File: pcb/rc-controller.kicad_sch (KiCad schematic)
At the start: 77 parts, among them J1 USB_C_Receptacle_USB2.0, M1 Motor_DC, Q1 AO3401A, Q2 AO3401A, Q3 AO3400A, Q4 AO3400A, SW1 SW_SPDT, SW2 SW_SPDT, SW3 SW_DPST, SW4 SW_DPST, SW5 SW_DPST, SW6 SW_DPST, U1 STM32F401RCTx, U2 LPS22HB, U3 SRV05-4, U4 TX4401, U5 ICM-42670-P, U6 TP4057-42, U7 nrf24L01P_PA_LNA, U8 SSD1306, Y1 16MHz

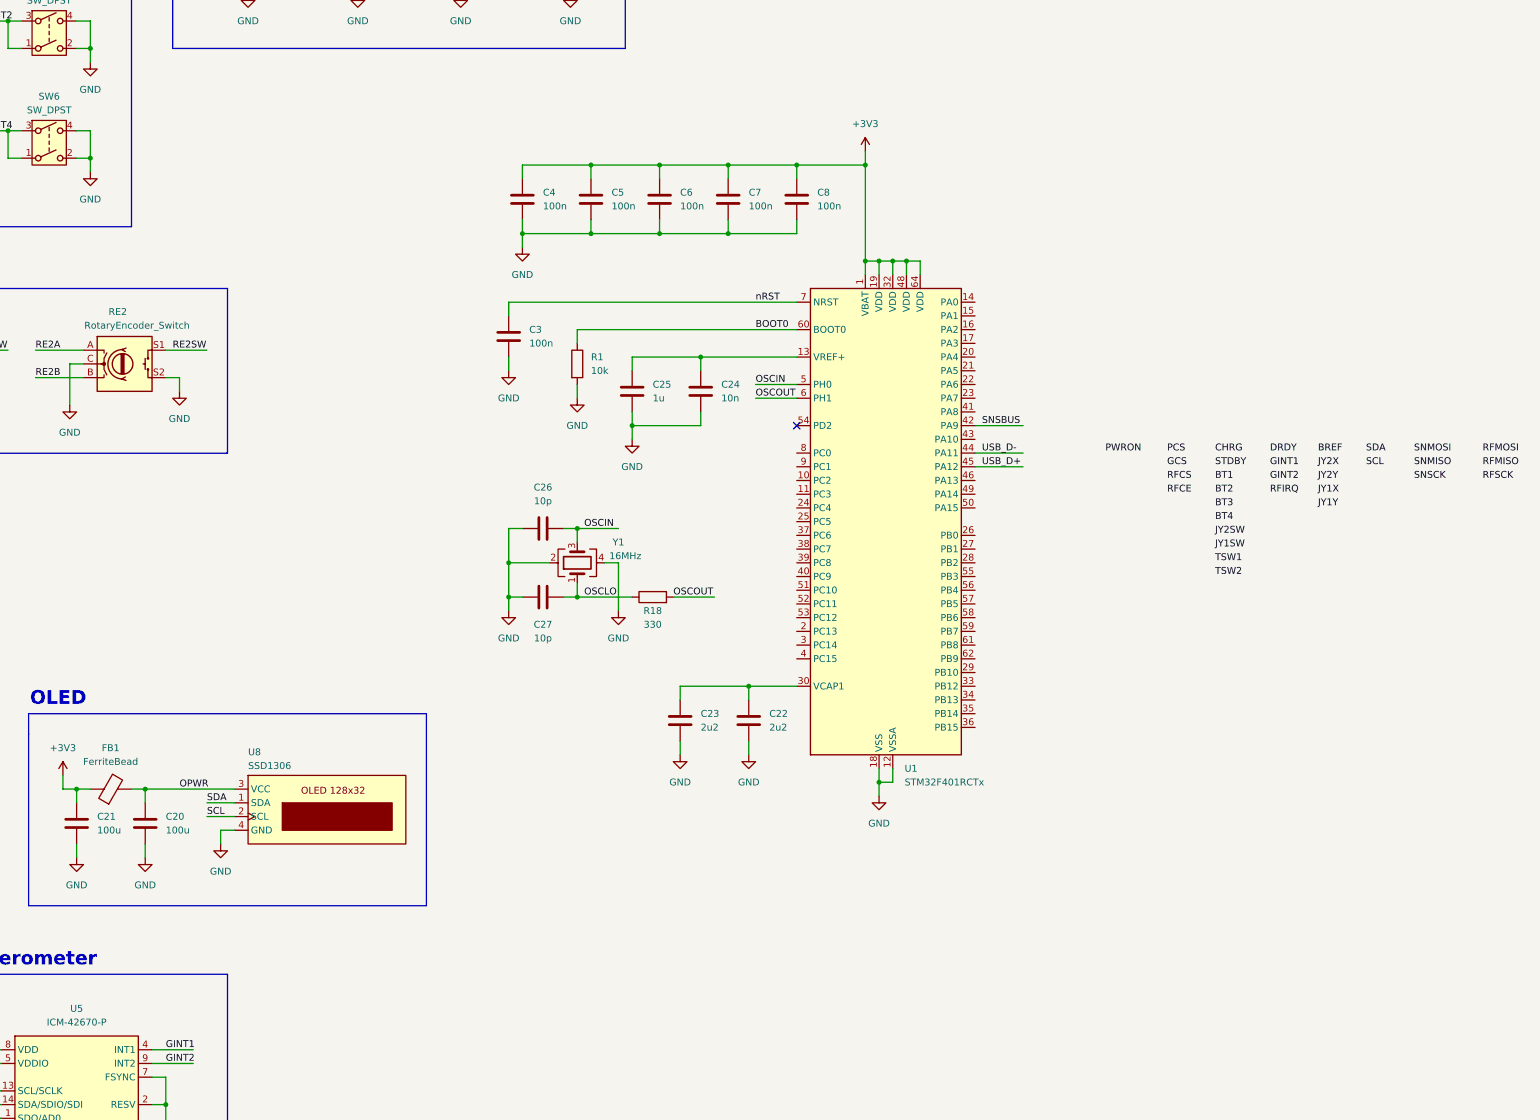
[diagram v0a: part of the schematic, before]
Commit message: Assign basic footprints
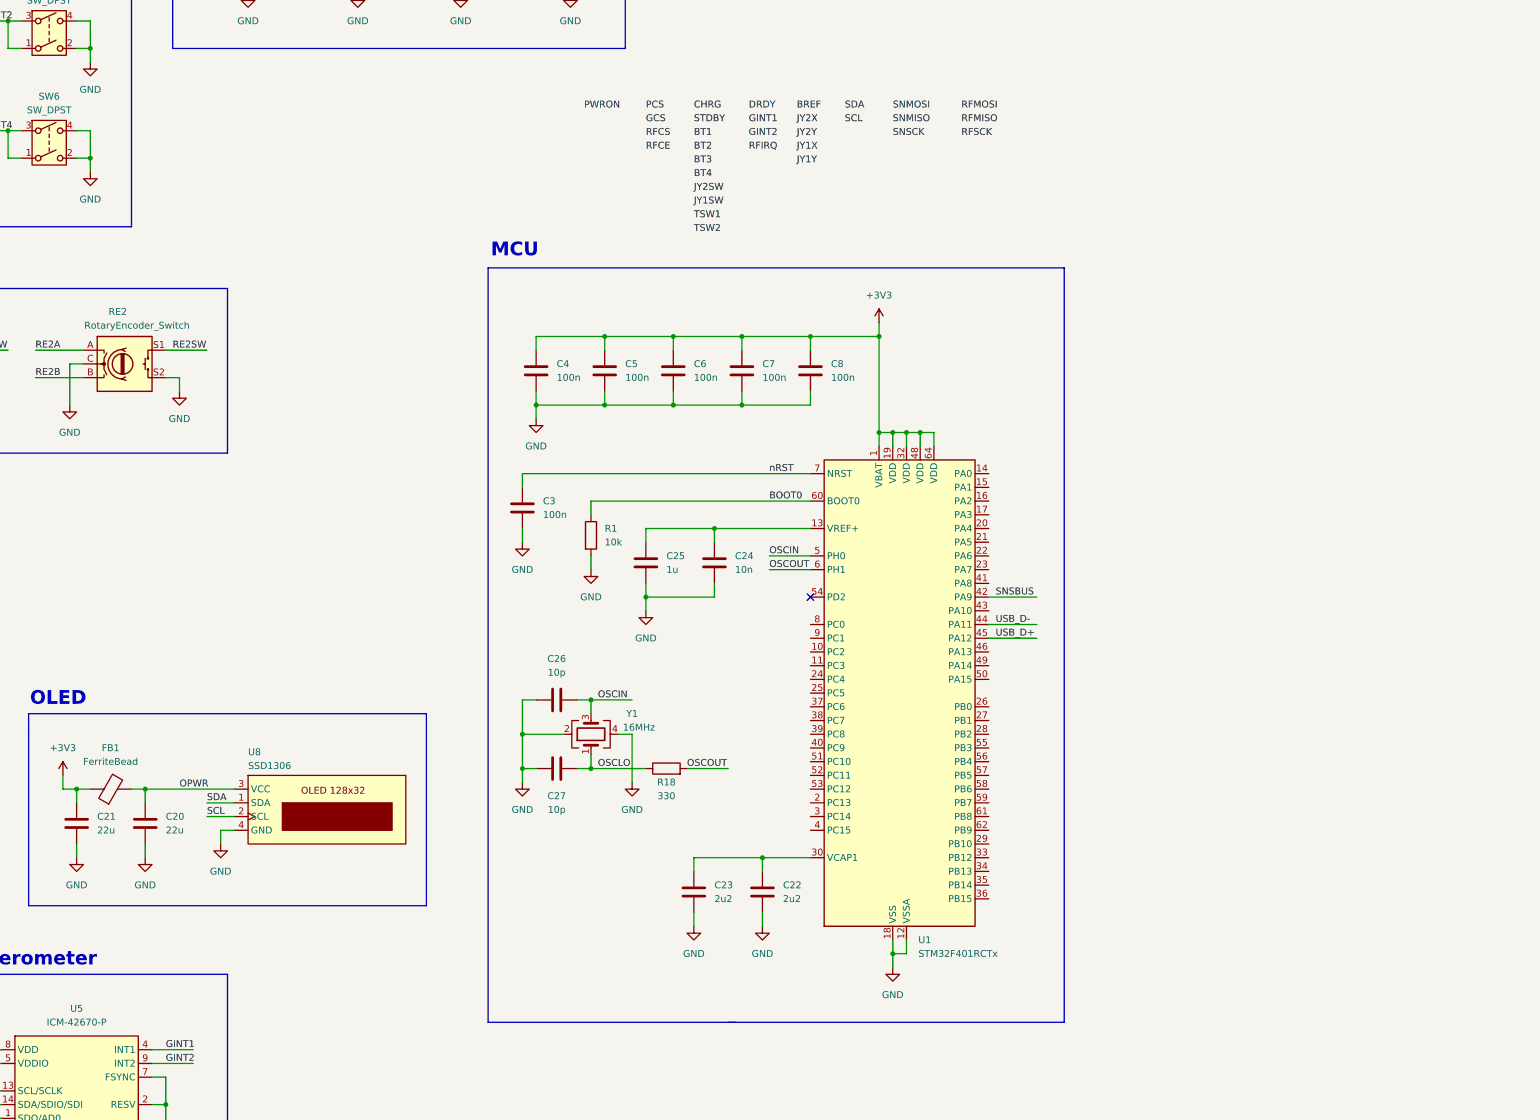
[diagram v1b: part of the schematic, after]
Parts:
- C1, C3, C4, C5, C6, C7, C8: footprint (none) -> Capacitor_SMD:C_0402_1005Metric
- C20, C21: value 100u -> 22u
- R11, R12, R13, R14, R16, R17, R9: footprint (none) -> Resistor_SMD:R_0402_1005Metric
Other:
- note added: "MCU"
- moved on the sheet: C22, C23, C24, C25, C26, C27, C3, C4, C5, C6, C7, C8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

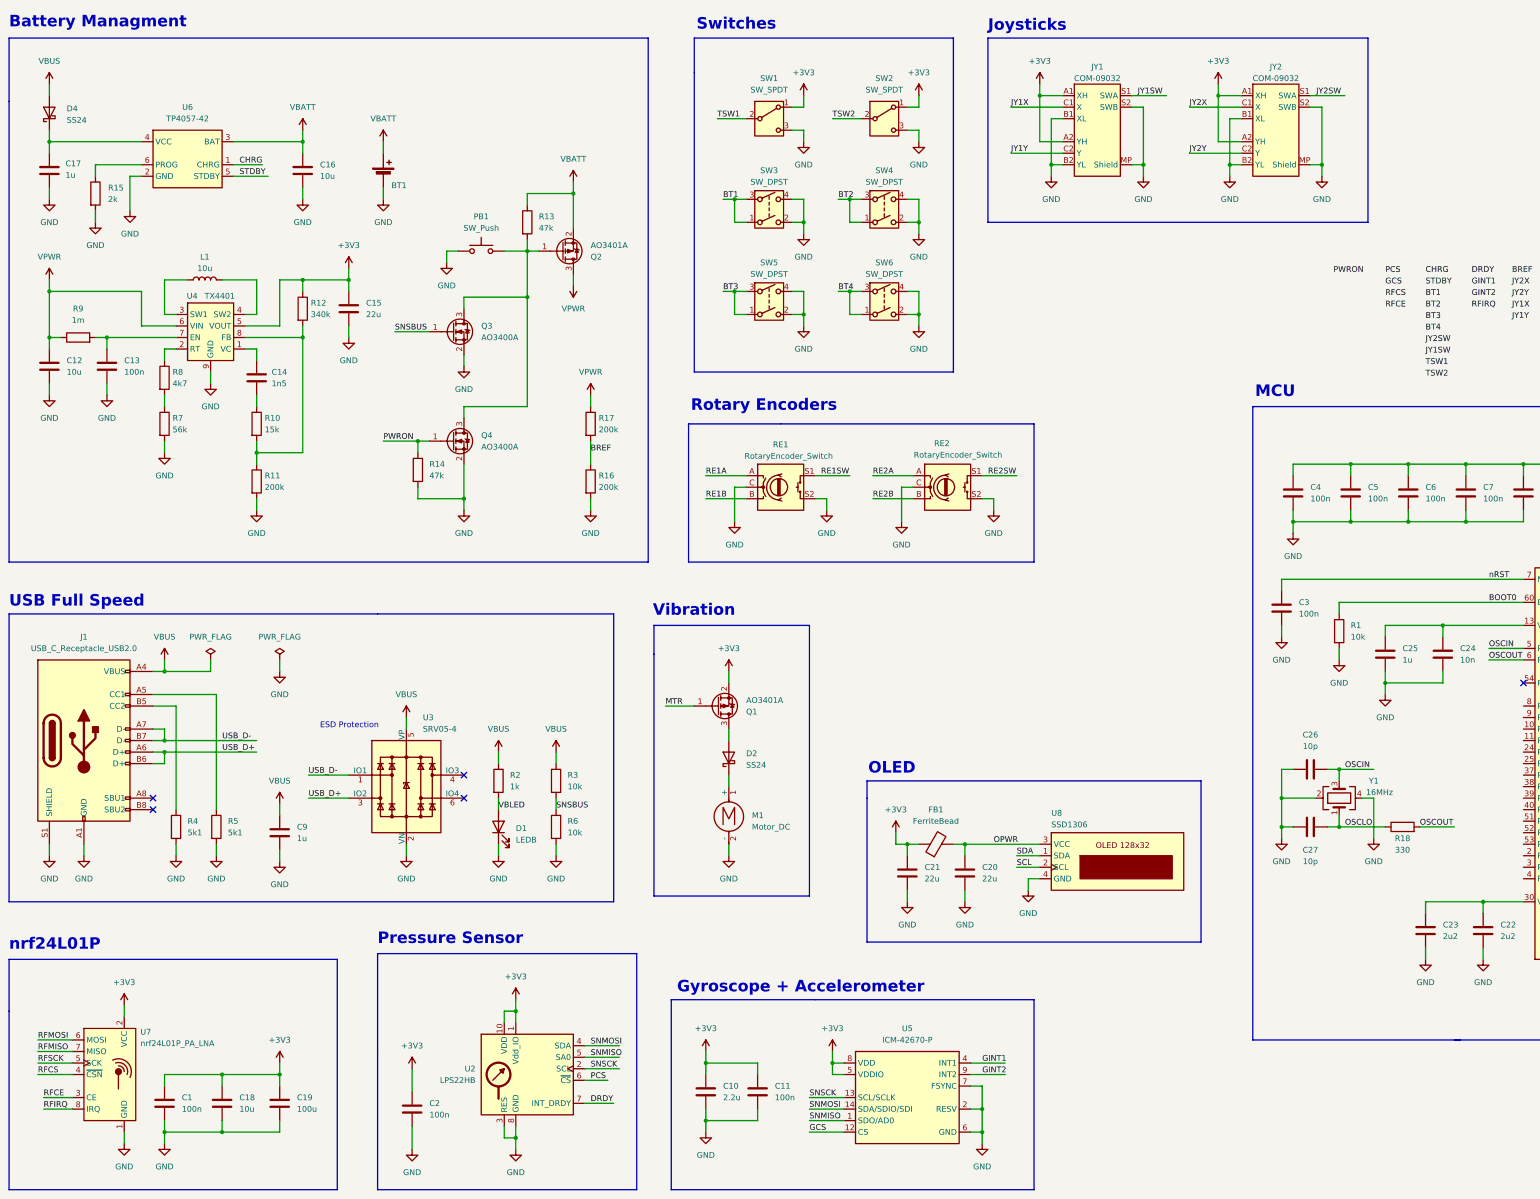
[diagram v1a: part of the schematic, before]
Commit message: Finish mapping footprints
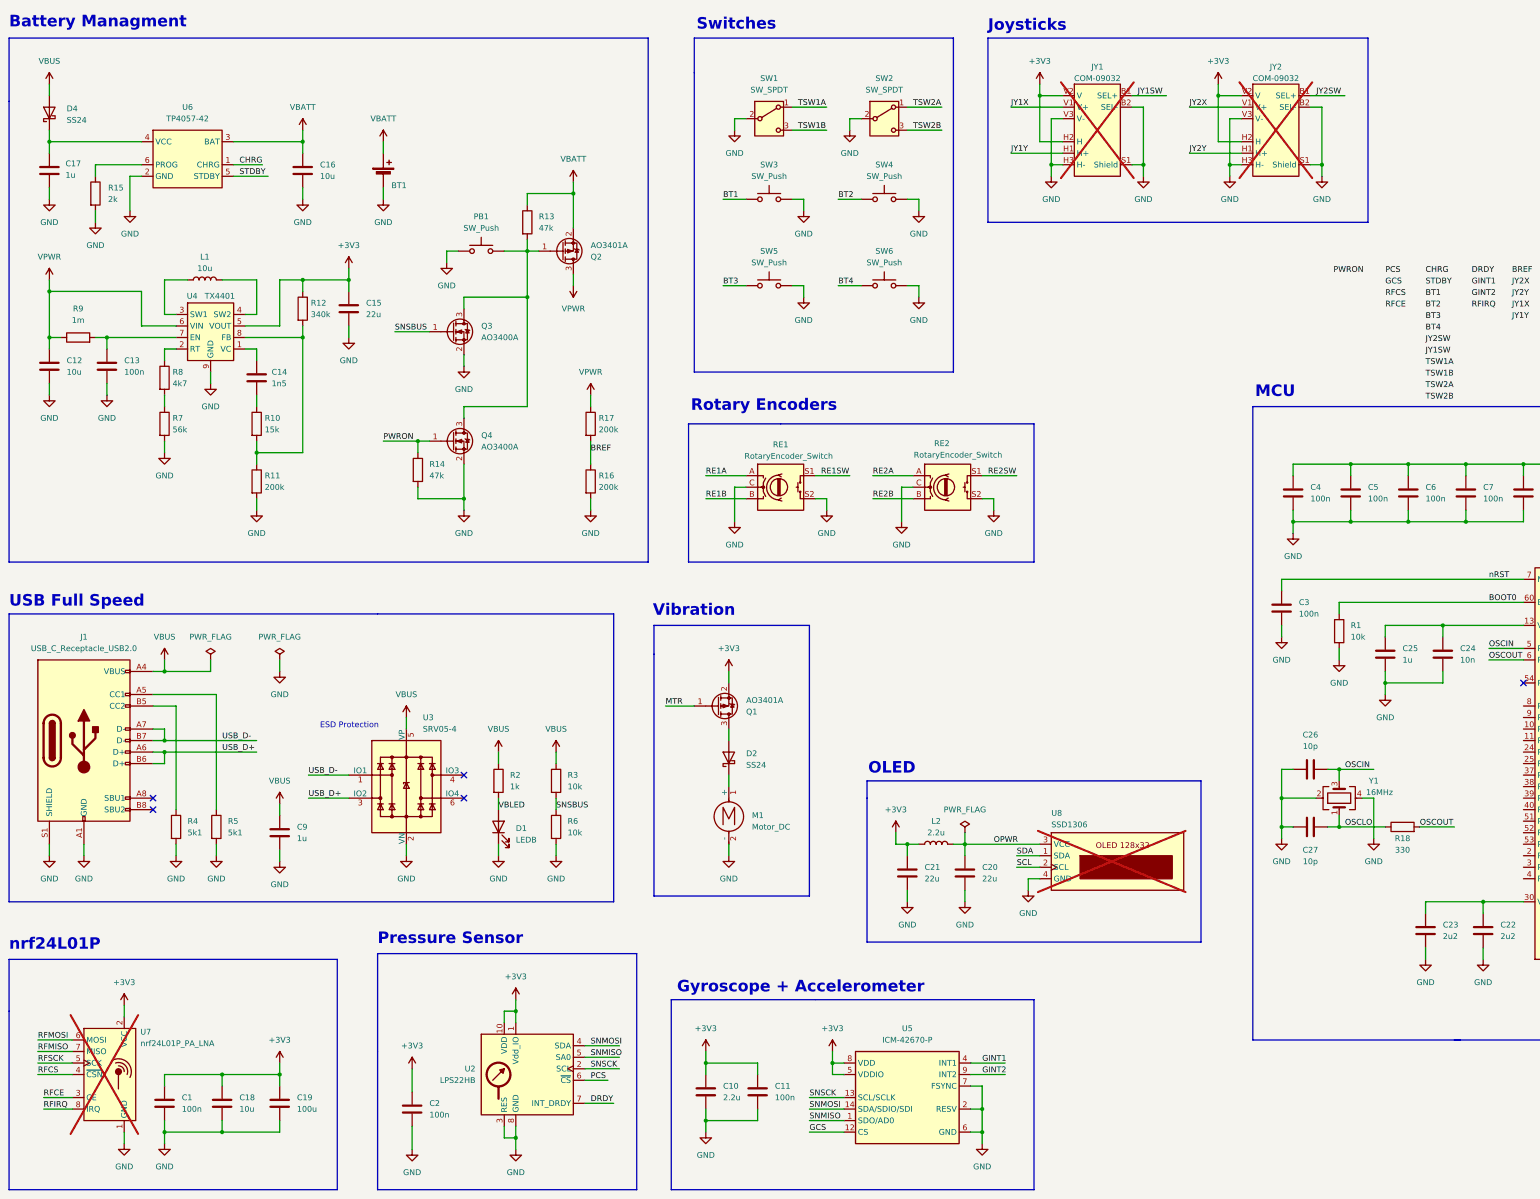
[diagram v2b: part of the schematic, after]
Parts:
- removed FB1: FerriteBead, symbol Device:FerriteBead
- removed SW3, SW4, SW5, SW6: SW_DPST, symbol Switch:SW_DPST
- added L2: 2.2u, Inductor_SMD:L_0805_2012Metric, symbol Device:L
- added SW3, SW4, SW5, SW6: SW_Push, Button_Switch_THT:SW_PUSH_6mm_H13mm, symbol Switch:SW_Push
- BT1: footprint (none) -> Connector_PinHeader_2.54mm:PinHeader_1x02_P2.54mm_Vertical
- C12: footprint (none) -> Capacitor_SMD:C_0603_1608Metric; LCSC (none) -> C19702
- C13, C14, C17, C22, C23, C24, C25: footprint (none) -> Capacitor_SMD:C_0402_1005Metric
- C15, C16, C18, C20, C21: footprint (none) -> Capacitor_SMD:C_0603_1608Metric
- C19: footprint (none) -> Capacitor_SMD:C_1206_3216Metric
- JY1, JY2: footprint (none) -> User_Footprints:COM-09032; now not fitted
- L1: footprint (none) -> Inductor_SMD:L_1206_3216Metric; LCSC (none) -> C395029
- M1: footprint (none) -> Motors:Vybronics_VZ30C1T8219732L
- PB1: footprint (none) -> Button_Switch_THT:SW_PUSH_6mm_H13mm; LCSC (none) -> C2834892
- R1, R10, R15, R7, R8: footprint (none) -> Resistor_SMD:R_0402_1005Metric
- RE1, RE2: footprint (none) -> Rotary_Encoder:RotaryEncoder_Alps_EC11E-Switch_Vertical_H20mm; LCSC (none) -> C202365
- SW1, SW2: footprint (none) -> User_Footprints:2MS; LCSC (none) -> C908281
- U7: footprint (none) -> Connector_PinHeader_2.54mm:PinHeader_2x04_P2.54mm_Vertical; now not fitted
- U8: footprint (none) -> Connector_PinHeader_2.54mm:PinHeader_1x04_P2.54mm_Vertical; now not fitted
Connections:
- net TSW1 is gone; now on net GND: SW1.2 (B)
- net TSW2 is gone; now on net GND: SW2.2 (B)
- net +3V3: now also JY1.H2 (H), JY1.V2 (V), JY2.H2 (H), JY2.V2 (V), L2.1; no longer JY1.A1 (XH), JY1.A2 (YH), JY2.A1 (XH), JY2.A2 (YH), SW1.1 (A), SW2.1 (A)
- net BT1: now also SW3.1
- net BT2: now also SW4.1
- net BT3: now also SW5.1
- net BT4: now also SW6.1
- net GND: now also JY1.H3 (H-), JY1.S1 (Shield), JY1.V3 (V-), JY2.H3 (H-), JY2.S1 (Shield), JY2.V3 (V-), SW3.2, SW4.2, SW5.2, SW6.2; no longer JY1.B1 (XL), JY1.MP (Shield), JY1.S2 (SWB), JY2.B1 (XL), JY2.MP (Shield), JY2.S2 (SWB), SW1.3 (C), SW2.3 (C)
- net JY1SW: now also JY1.B1 (SEL+); no longer JY1.S1 (SWA)
- net JY1X: now also JY1.V1 (V+); no longer JY1.C1 (X)
- net JY1Y: now also JY1.H1 (H+); no longer JY1.C2 (Y)
- net JY2SW: now also JY2.B1 (SEL+); no longer JY2.S1 (SWA)
- net JY2X: now also JY2.V1 (V+); no longer JY2.C1 (X)
- net JY2Y: now also JY2.H1 (H+); no longer JY2.C2 (Y)
- net OPWR: now also L2.2
- new net TSW1A: SW1.1 (A)
- new net TSW1B: SW1.3 (C)
- new net TSW2A: SW2.1 (A)
- new net TSW2B: SW2.3 (C)

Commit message: Final placement before routing
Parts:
- removed J1: USB_C_Receptacle_USB2.0, Connector_USB:USB_C_Receptacle_GCT_USB4105-xx-A_16P_TopMnt_Horizontal, symbol Connector:USB_C_Receptacle_USB2.0
- removed U5: ICM-42670-P, Package_LGA:LGA-14_3x2.5mm_P0.5mm_LayoutBorder3x4y, symbol MySymbols:ICM-42670-P
- added C28: 10u, Capacitor_SMD:C_0402_1005Metric, symbol Device:C
- added J2: USB_C_Receptacle_USB2.0_16P, Connector_USB:USB_C_Receptacle_GCT_USB4105-xx-A_16P_TopMnt_Horizontal, symbol Connector:USB_C_Receptacle_USB2.0_16P
- added JP1: Jumper_2_Open, Jumper:SolderJumper-2_P1.3mm_Open_RoundedPad1.0x1.5mm, symbol Jumper:Jumper_2_Open
- added U5: ICM-42670-P, Package_LGA:LGA-14_3x2.5mm_P0.5mm_LayoutBorder3x4y, symbol User_Symbols:ICM-42670-P
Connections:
- net +3V3: now also JY1.A1 (XH), JY1.A2 (YH), JY2.A1 (XH), JY2.A2 (YH), C28.1, U5.5 (VDDIO), U5.8 (VDD); no longer JY1.H2 (H), JY1.V2 (V), JY2.H2 (H), JY2.V2 (V)
- net GCS: now also U5.12 (CS)
- net GINT1: now also U5.4 (INT1)
- net GND: now also JY1.B1 (XL), JY1.MP (Shield), JY1.S2 (SWB), JY2.B1 (XL), JY2.MP (Shield), JY2.S2 (SWB), C28.2, J2.A1 (GND), J2.A12 (GND), J2.B1 (GND), J2.B12 (GND), J2.S1 (SHIELD), JP1.1 (A), U5.10 (RESV), U5.11 (RESV), U5.2 (RESV), U5.3 (RESV), U5.6 (GND), U5.7 (FSYNC); no longer JY1.H3 (H-), JY1.S1 (Shield), JY1.V3 (V-), JY2.H3 (H-), JY2.S1 (Shield), JY2.V3 (V-)
- net JY1SW: now also JY1.S1 (SWA); no longer JY1.B1 (SEL+)
- net JY1X: now also JY1.C1 (X); no longer JY1.V1 (V+)
- net JY1Y: now also JY1.C2 (Y); no longer JY1.H1 (H+)
- net JY2SW: now also JY2.S1 (SWA); no longer JY2.B1 (SEL+)
- net JY2X: now also JY2.C1 (X); no longer JY2.V1 (V+)
- net JY2Y: now also JY2.C2 (Y); no longer JY2.H1 (H+)
- net SNMISO: now also U5.1 (SDO/AD0)
- net SNMOSI: now also U5.14 (SDA/SDIO/SDI)
- net SNSCK: now also U5.13 (SCL/SCLK)
- net USB_D+: now also J2.A6 (D+), J2.B6 (D+)
- net USB_D-: now also J2.A7 (D-), J2.B7 (D-)
- net VBUS: now also J2.A4 (VBUS), J2.A9 (VBUS), J2.B4 (VBUS), J2.B9 (VBUS)
- net VREF: now reaches C24.1, C25.1, U1.13 (VREF+)
- net VCAP: now reaches C22.1, C23.1, U1.30 (VCAP1)
- net at C13.1, R9.2, U4.7 (EN): now also JP1.2 (B)
- net at R5.1: now also J2.A5 (CC1)
- net at R4.1: now also J2.B5 (CC2)
- no-connect marks 5 -> 6
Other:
- moved on the sheet: C12, C13, C22, C23, C24, C25, C26, C27, C3, C4, C5, C6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
